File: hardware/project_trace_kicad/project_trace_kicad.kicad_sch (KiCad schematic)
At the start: 0 parts

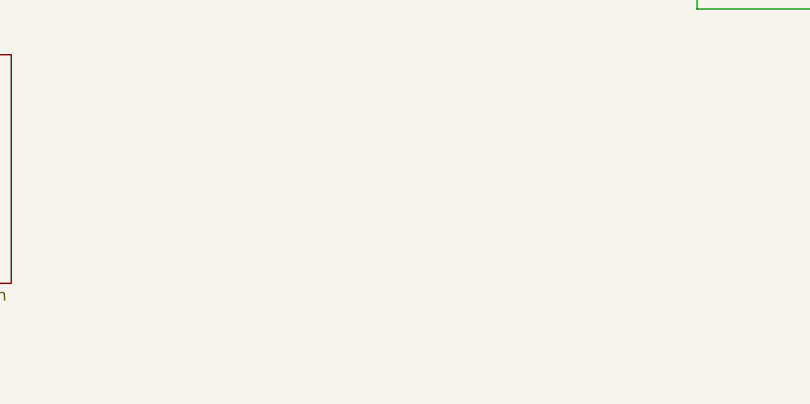
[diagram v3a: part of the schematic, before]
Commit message: Review 1 issues adressed
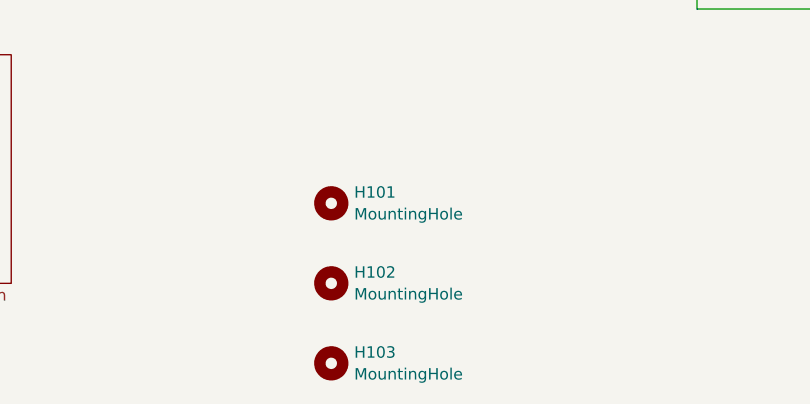
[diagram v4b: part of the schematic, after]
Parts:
- added H101, H102, H103: MountingHole, MountingHole:MountingHole_4.3mm_M4_DIN965, symbol Mechanical:MountingHole
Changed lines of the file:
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@@
+		)
+	)
+	(symbol
+		(lib_id "Mechanical:MountingHole")
+		(at 105.41 137.16 0)
+		(unit 1)
+		(body_style 1)
+		(exclude_from_sim no)
+		(in_bom no)
+		(on_board yes)
+		(in_pos_files yes)
+		(dnp no)
+		(fields_autoplaced yes)
+		(property "Reference" "H101"
+			(at 107.95 135.9478 0)
+			(show_name no)
+			(do_not_autoplace no)
+			(effects
+				(font
+					(size 1.27 1.27)
+				)
+				(justify left)
+			)
+		)
+		(property "Value" "MountingHole"
+			(at 107.95 138.3721 0)
+			(show_name no)
+			(do_not_autoplace no)
+			(effects
+				(font
+					(size 1.27 1.27)
+				)
+				(justify left)
+			)
+		)
+		(property "Footprint" "MountingHole:MountingHole_4.3mm_M4_DIN965"
+			(at 105.41 137.16 0)
+			(hide yes)
+			(show_name no)
+			(do_not_autoplace no)
+			(effects
+				(font
+					(size 1.27 1.27)
+				)
+			)
+		)
+		(property "Datasheet" ""
+			(at 105.41 137.16 0)
+			(hide yes)
+			(show_name no)
+			(do_not_autoplace no)
+			(effects
+				(font
+					(size 1.27 1.27)
+				)
+			)
+		)
+		(property "Description" "Mounting Hole without connection"
+			(at 105.41 137.16 0)
+			(hide yes)
+			(show_name no)
+			(do_not_autoplace no)
+			(effects
+				(font
+					(size 1.27 1.27)
+				)
+			)
+		)
+		(instances
+			(project "project_trace_kicad"
+				(path "/af51f4e5-b952-4b0e-baf2-78a72fb86fcd"
+					(reference "H101")
+					(unit 1)
+				)
+			)
+		)
+	)
+	(symbol
+		(lib_id "Mechanical:MountingHole")
+		(at 105.41 154.94 0)
+		(unit 1)
+		(body_style 1)
+		(exclude_from_sim no)
+		(in_bom no)
+		(on_board yes)
+		(in_pos_files yes)
+		(dnp no)
+		(fields_autoplaced yes)
+		(property "Reference" "H103"
+			(at 107.95 153.7278 0)
+			(show_name no)
+			(do_not_autoplace no)
+			(effects
+				(font
+					(size 1.27 1.27)
+				)
+				(justify left)
+			)
+		)
+		(property "Value" "MountingHole"
+			(at 107.95 156.1521 0)
+			(show_name no)
+			(do_not_autoplace no)
+			(effects
+				(font
+					(size 1.27 1.27)
+				)
+				(justify left)
+			)
+		)
+		(property "Footprint" "MountingHole:MountingHole_4.3mm_M4_DIN965"
+			(at 105.41 154.94 0)
+			(hide yes)
+			(show_name no)
+			(do_not_autoplace no)
+			(effects
+				(font
+					(size 1.27 1.27)
+				)
+			)
+		)
+		(property "Datasheet" ""
+			(at 105.41 154.94 0)
+			(hide yes)
+			(show_name no)
+			(do_not_autoplace no)
+			(effects
+				(font
+					(size 1.27 1.27)
+				)
+			)
+		)
+		(property "Description" "Mounting Hole without connection"
+			(at 105.41 154.94 0)
+			(hide yes)
+			(show_name no)
+			(do_not_autoplace no)
+			(effects
+				(font
+					(size 1.27 1.27)
+				)
+			)
+		)
+		(instances
+			(project "project_trace_kicad"
+				(path "/af51f4e5-b952-4b0e-baf2-78a72fb86fcd"
+					(reference "H103")
+					(unit 1)
+				)
+			)
+		)
+	)
+	(symbol
+		(lib_id "Mechanical:MountingHole")
+		(at 105.41 146.05 0)
+		(unit 1)
+		(body_style 1)
+		(exclude_from_sim no)
+		(in_bom no)
+		(on_board yes)
+		(in_pos_files yes)
+		(dnp no)
+		(fields_autoplaced yes)
+		(property "Reference" "H102"
+			(at 107.95 144.8378 0)
+			(show_name no)
+			(do_not_autoplace no)
+			(effects
+				(font
+					(size 1.27 1.27)
+				)
+				(justify left)
+			)
+		)
+		(property "Value" "MountingHole"
+			(at 107.95 147.2621 0)
+			(show_name no)
+			(do_not_autoplace no)
+			(effects
+				(font
+					(size 1.27 1.27)
+				)
+				(justify left)
+			)
+		)
+		(property "Footprint" "MountingHole:MountingHole_4.3mm_M4_DIN965"
+			(at 105.41 146.05 0)
+			(hide yes)
+			(show_name no)
+			(do_not_autoplace no)
+			(effects
+				(font
+					(size 1.27 1.27)
+				)
+			)
+		)
+		(property "Datasheet" ""
+			(at 105.41 146.05 0)
+			(hide yes)
+			(show_name no)
+			(do_not_autoplace no)
+			(effects
+				(font
+					(size 1.27 1.27)
+				)
+			)
+		)
+		(property "Description" "Mounting Hole without connection"
+			(at 105.41 146.05 0)
+			(hide yes)
+			(show_name no)
+			(do_not_autoplace no)
+			(effects
+				(font
+					(size 1.27 1.27)
+				)
+			)
+		)
+		(instances
+			(project "project_trace_kicad"
+				(path "/af51f4e5-b952-4b0e-baf2-78a72fb86fcd"
+					(reference "H102")
+					(unit 1)
+				)
+			)
 		)
 	)

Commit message: Address items of internal review
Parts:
- H101, H102, H103: DigikeyPN (none) -> N/A
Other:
- sheet Measurement and Analysis Module ports: added Range.Gain.20dB; removed Range.Gain.~{20dB}
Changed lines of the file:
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@@
 	(title_block
 		(title "Multilloscope")
+		(date "2026-04-19")
 		(comment 1 "Marius H. Tyson")
 		(comment 2 "Alexander N. Olsen")
@@
 			)
 		)
+		(property "DigikeyPN" "N/A"
+			(at 105.41 137.16 0)
+			(hide yes)
+			(show_name no)
+			(do_not_autoplace no)
+			(effects
+				(font
+					(size 1.27 1.27)
+				)
+			)
+		)
 		(instances
 			(project "project_trace_kicad"
@@
 			)
 		)
+		(property "DigikeyPN" "N/A"
+			(at 105.41 154.94 0)
+			(hide yes)
+			(show_name no)
+			(do_not_autoplace no)
+			(effects
+				(font
+					(size 1.27 1.27)
+				)
+			)
+		)
 		(instances
 			(project "project_trace_kicad"
@@
 			)
 		)
+		(property "DigikeyPN" "N/A"
+			(at 105.41 146.05 0)
+			(hide yes)
+			(show_name no)
+			(do_not_autoplace no)
+			(effects
+				(font
+					(size 1.27 1.27)
+				)
+			)
+		)
 		(instances
 			(project "project_trace_kicad"
@@
 			)
 		)
-		(pin "Range.Gain.~{20dB}" output
-			(at 120.65 62.23 180)
-			(effects
-				(font
-					(size 1.27 1.27)
-				)
-				(justify left)
-			)
-		)
 		(pin "VOLT{slash}~{AMP}" output
 			(at 120.65 54.61 180)
 			(effects
 				(font
+					(size 1.27 1.27)
+				)
+				(justify left)
+			)
+		)
+		(pin "Range.Gain.20dB" output
+			(at 120.65 62.23 180)
+			(effects
+				(font
